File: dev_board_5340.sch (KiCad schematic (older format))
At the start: 41 parts, among them J1 Conn_01x04_Male, J2 USB_C_Receptacle_USB2.0, U1 nrf5340, U2 USBLC6-2SC6, U3 W25Q128JVS, Y1 Crystal_GND2_Small

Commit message: change schematic
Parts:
- added AE?: Antenna, symbol Device:Antenna
- added C? (x8): C_Small, symbol Device:C_Small
- added J?: Conn_01x02_Male, symbol Connector:Conn_01x02_Male
- added L? (x2): INDUCTOR, symbol pspice:INDUCTOR
- added R? (x3): R_Small, symbol Device:R_Small
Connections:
- net labels added: B_LED, DCC, G_LED, R_LED, USER_BUT
- wire segments 174 -> 213
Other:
- moved on the sheet: AE1, C?, D1, R1, R2, R3, R?, SW?, Y?

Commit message: change schematic
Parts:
- added C14, C25, C26, C27, C? (x3): C_Small, symbol Device:C_Small
- added D? (x3): LED, symbol Device:LED
- added J? (x2): Conn_01x24, symbol Connector_Generic:Conn_01x24
- added R? (x3): R_Small, symbol Device:R_Small
- added U4, U?: AZ1117-3.3, symbol Regulator_Linear:AZ1117-3.3
- gave numbers to parts that had none: 22
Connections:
- net labels added: +VDC, P0.10, P0.11, P0.12, P0.23, P0.24, P0.25, P0.26, P0.27, P0.28, P0.29, P0.30, P0.31, P0.4, P0.5, P0.6, P0.7, P0.8, P0.9, P1.0, P1.1, P1.10, P1.11, P1.12, P1.13, P1.14, P1.15, P1.2, P1.3, P1.4, P1.5, P1.6, P1.7, P1.8, P1.9
- wire segments 213 -> 346
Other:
- moved on the sheet: D1, D2, D3, D4, F1, J2, R1, R13, R2, R3, R4, R5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

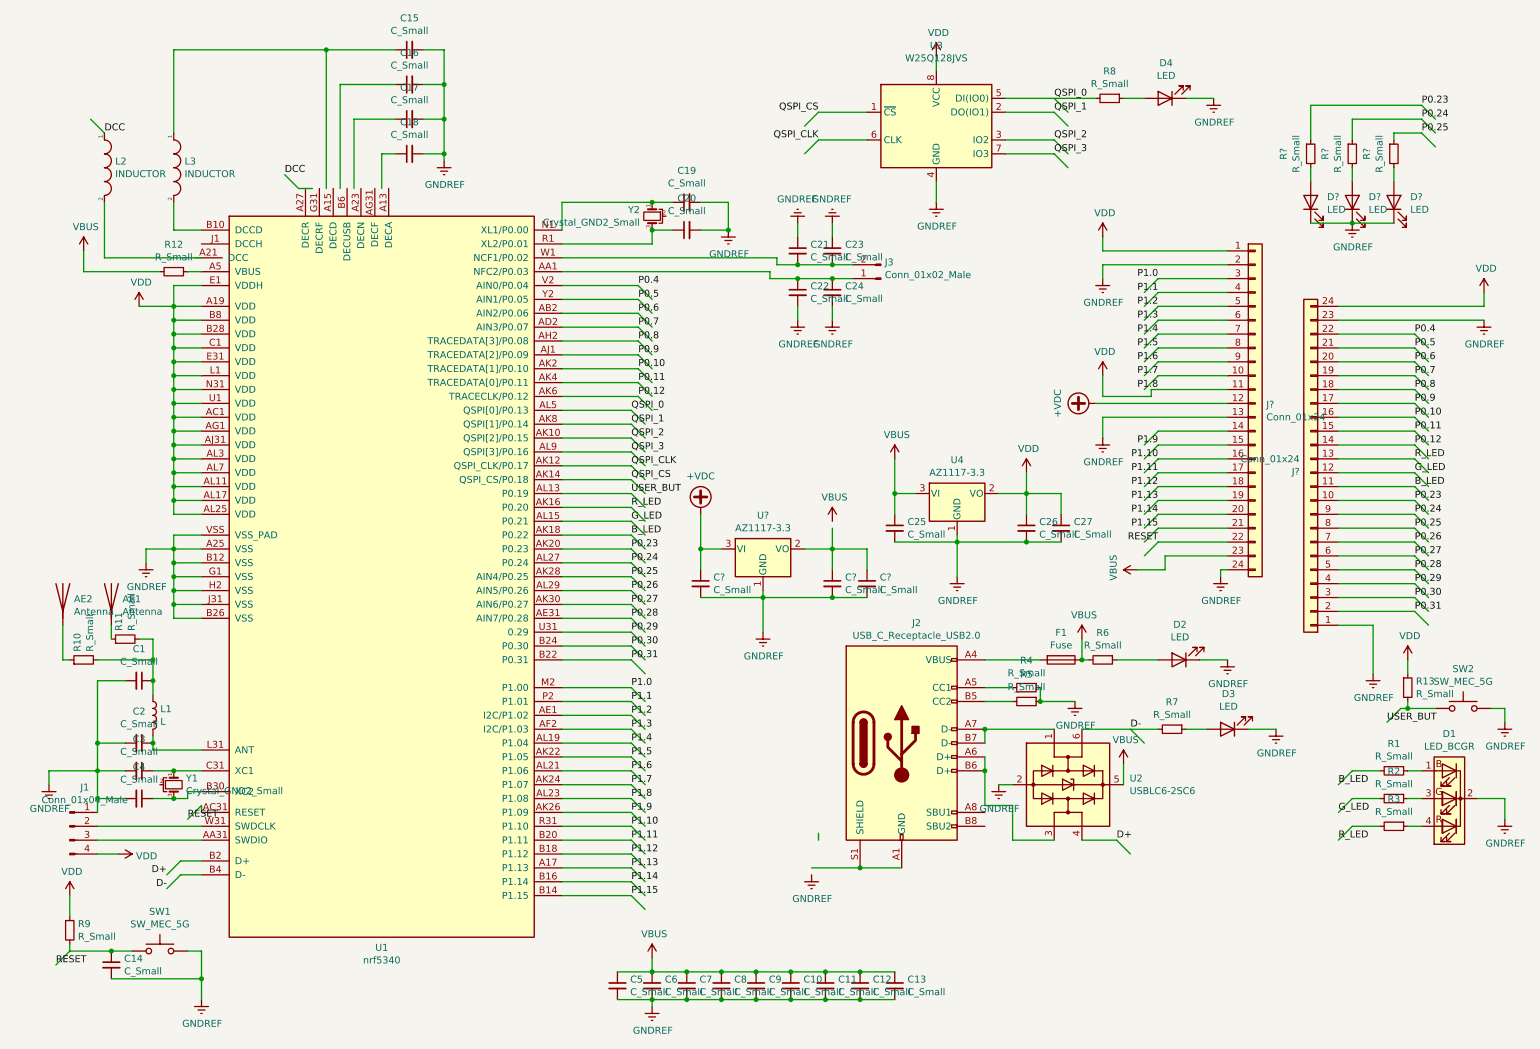
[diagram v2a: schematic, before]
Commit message: add footprint and rating for each component
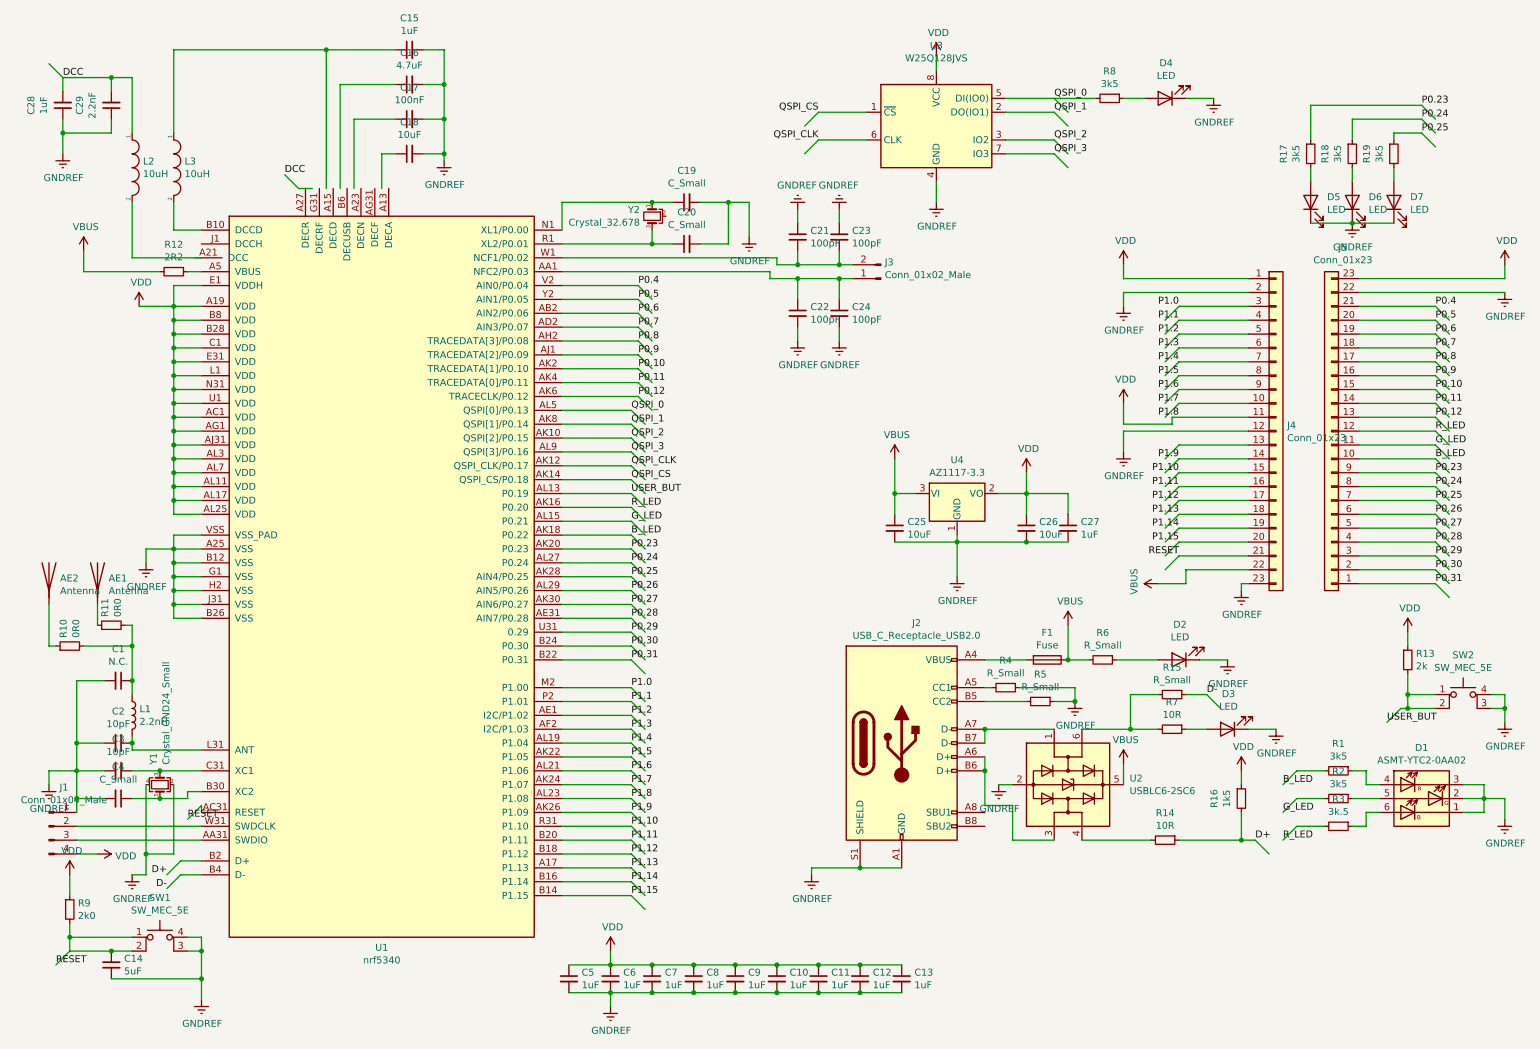
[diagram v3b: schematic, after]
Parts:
- removed C? (x3): C_Small, symbol Device:C_Small
- removed D1: LED_BCGR, symbol Device:LED_BCGR
- removed J? (x2): Conn_01x24, symbol Connector_Generic:Conn_01x24
- removed SW1, SW2: SW_MEC_5G, symbol Switch:SW_MEC_5G
- removed U?: AZ1117-3.3, symbol Regulator_Linear:AZ1117-3.3
- removed Y1: Crystal_GND2_Small, symbol Device:Crystal_GND2_Small
- added C28: 1uF, Capacitor_SMD:C_0805_2012Metric, symbol Device:C_Small
- added C29: 2.2nF, Capacitor_SMD:C_0805_2012Metric, symbol Device:C_Small
- added D1: ASMT-YTC2-0AA02, LED_SMD:LED_Avago_PLCC6_3x2.8mm, symbol LED:ASMT-YTC2-0AA02
- added J4, J5: Conn_01x23, Connector_PinHeader_2.54mm:PinHeader_1x23_P2.54mm_Vertical, symbol Connector_Generic:Conn_01x23
- added R14: 10R, Resistor_SMD:R_1206_3216Metric, symbol Device:R_Small
- added R15: R_Small, Resistor_SMD:R_1206_3216Metric, symbol Device:R_Small
- added R16: 1k5, Capacitor_SMD:C_0805_2012Metric, symbol Device:R_Small
- added SW1, SW2: SW_MEC_5E, Button_Switch_SMD:SW_Push_1P1T_NO_CK_KSC6xxJ, symbol Switch:SW_MEC_5E
- added Y1: Crystal_GND24_Small, Crystal:Crystal_SMD_3225-4Pin_3.2x2.5mm, symbol Device:Crystal_GND24_Small
- AE1: footprint (none) -> RF_Antenna:Texas_SWRA117D_2.4GHz_Left
- AE2: footprint (none) -> Connector_Coaxial:U.FL_Hirose_U.FL-R-SMT-1_Vertical
- C1: value C_Small -> N.C.; footprint (none) -> Capacitor_SMD:C_0805_2012Metric
- C10, C11, C12, C13, C15, C27, C5, C6, C7, C8, C9: value C_Small -> 1uF; footprint (none) -> Capacitor_SMD:C_0805_2012Metric
- C14: value C_Small -> 5uF; footprint (none) -> Capacitor_SMD:C_0805_2012Metric
- C16: value C_Small -> 4.7uF; footprint (none) -> Capacitor_SMD:C_0805_2012Metric
- C17: value C_Small -> 100nF; footprint (none) -> Capacitor_SMD:C_0805_2012Metric
- C18: value C_Small -> 10uF; footprint (none) -> Capacitor_SMD:C_0805_2012Metric
- C19, C20, C4: footprint (none) -> Capacitor_SMD:C_0805_2012Metric
- C2, C3: value C_Small -> 10pF; footprint (none) -> Capacitor_SMD:C_0805_2012Metric
- C21, C22, C23, C24: value C_Small -> 100pF; footprint (none) -> Capacitor_SMD:C_0805_2012Metric
- C25, C26: value C_Small -> 10uF; footprint (none) -> Capacitor_SMD:C_1206_3216Metric
- D2, D3, D4: footprint (none) -> Diode_SMD:D_0805_2012Metric
- D5, D6, D7: renamed from D?; footprint (none) -> Diode_SMD:D_0805_2012Metric
- F1: footprint (none) -> Fuse:Fuse_1206_3216Metric
- J1: footprint (none) -> Connector_PinHeader_2.54mm:PinHeader_1x04_P2.54mm_Vertical
- J2: footprint (none) -> Connector_USB:USB_C_Receptacle_XKB_U262-16XN-4BVC11
- J3: footprint (none) -> Connector_PinHeader_2.54mm:PinHeader_1x02_P2.54mm_Vertical
- L1: value L -> 2.2nH; footprint (none) -> Inductor_SMD:L_1206_3216Metric
- L2, L3: value INDUCTOR -> 10uH; footprint (none) -> Inductor_SMD:L_1206_3216Metric
- R1, R2, R8: value R_Small -> 3k5; footprint (none) -> Resistor_SMD:R_0805_2012Metric
- R10, R11: value R_Small -> 0R0; footprint (none) -> Resistor_SMD:R_0402_1005Metric
- R12: value R_Small -> 2R2; footprint (none) -> Resistor_SMD:R_1206_3216Metric
- R13: value R_Small -> 2k; footprint (none) -> Capacitor_SMD:C_0805_2012Metric
- R17, R18, R19: renamed from R?; value R_Small -> 3k5; footprint (none) -> Resistor_SMD:R_0805_2012Metric
- R3: value R_Small -> 3k.5; footprint (none) -> Resistor_SMD:R_0805_2012Metric
- R4, R5: footprint (none) -> Resistor_SMD:R_0805_2012Metric
- R6: footprint (none) -> Resistor_SMD:R_1206_3216Metric
- R7: value R_Small -> 10R; footprint (none) -> Capacitor_SMD:C_0805_2012Metric
- R9: value R_Small -> 2k0; footprint (none) -> Resistor_SMD:R_0805_2012Metric
- U4: footprint (none) -> Package_TO_SOT_SMD:SOT-223
- Y2: value Crystal_GND2_Small -> Crystal_32.678; footprint (none) -> Crystal:Crystal_SMD_3215-2Pin_3.2x1.5mm
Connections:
- net B_LED: now also J5.10 (Pin_10)
- net D+: now also R14.1, R16.2; no longer U2.4 (I/O2)
- net D-: now also R15.1; no longer R7.2, U2.6 (I/O1)
- net DCC: now also C28.2, C29.2
- net GNDREF: now also J2.A1 (GND), J2.A12 (GND), J2.B1 (GND), J2.B12 (GND), J2.S1 (SHIELD), C28.1, C29.1, D1.1 (KB), D1.2 (KG), D1.3 (KR), J4.12 (Pin_12), J4.2 (Pin_2), J4.23 (Pin_23), J5.22 (Pin_22), SW1.3 (K), SW1.4 (A), SW2.3 (K), SW2.4 (A), Y1.2, Y1.4
- net G_LED: now also J5.11 (Pin_11)
- net P0.10: now also J5.15 (Pin_15)
- net P0.11: now also J5.14 (Pin_14)
- net P0.12: now also J5.13 (Pin_13)
- net P0.23: now also J5.9 (Pin_9)
- net P0.24: now also J5.8 (Pin_8)
- net P0.25: now also J5.7 (Pin_7)
- net P0.26: now also J5.6 (Pin_6)
- net P0.27: now also J5.5 (Pin_5)
- net P0.28: now also J5.4 (Pin_4)
- net P0.29: now also J5.3 (Pin_3)
- net P0.30: now also J5.2 (Pin_2)
- net P0.31: now also J5.1 (Pin_1)
- net P0.4: now also J5.21 (Pin_21)
- net P0.5: now also J5.20 (Pin_20)
- net P0.6: now also J5.19 (Pin_19)
- net P0.7: now also J5.18 (Pin_18)
- net P0.8: now also J5.17 (Pin_17)
- net P0.9: now also J5.16 (Pin_16)
- net P1.0: now also J4.3 (Pin_3)
- net P1.1: now also J4.4 (Pin_4)
- net P1.10: now also J4.15 (Pin_15)
- net P1.11: now also J4.16 (Pin_16)
- net P1.12: now also J4.17 (Pin_17)
- net P1.13: now also J4.18 (Pin_18)
- net P1.14: now also J4.19 (Pin_19)
- net P1.15: now also J4.20 (Pin_20)
- net P1.2: now also J4.5 (Pin_5)
- net P1.3: now also J4.6 (Pin_6)
- net P1.4: now also J4.7 (Pin_7)
- net P1.5: now also J4.8 (Pin_8)
- net P1.6: now also J4.9 (Pin_9)
- net P1.7: now also J4.10 (Pin_10)
- net P1.9: now also J4.14 (Pin_14)
- net RESET: now also J4.21 (Pin_21)
- net R_LED: now also J5.12 (Pin_12)
- net VBUS: now also J4.22 (Pin_22); no longer C10.1, C11.1, C12.1, C13.1, C5.1, C6.1, C7.1, C8.1, C9.1
- net VDD: now also C10.1, C11.1, C12.1, C13.1, C5.1, C6.1, C7.1, C8.1, C9.1, J4.1 (Pin_1), J4.11 (Pin_11), J5.23 (Pin_23), R16.1
- net at C4.1, U1.B30 (XC2): now also Y1.1
- net at C3.1, U1.C31 (XC1): now also Y1.3
- net at R1.1: now also D1.4 (AR)
- net at R2.1: now also D1.5 (AG)
- net at R3.1: now also D1.6 (AB)
- net at C14.1, R9.2: now also SW1.1, SW1.2
- net at R13.2: now also SW2.1, SW2.2
- new net: R14.2, U2.4 (I/O2)
- new net: R15.2, R7.2, U2.6 (I/O1)
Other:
- moved on the sheet: AE1, AE2, C1, C10, C11, C12, C13, C2, C20, C21, C22, C23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

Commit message: Refactoring. Start trace
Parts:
- removed SW1, SW2: SW_MEC_5E, Button_Switch_SMD:SW_Push_1P1T_NO_CK_KSC6xxJ, symbol Switch:SW_MEC_5E
- removed Y2: Crystal_32.678, Crystal:Crystal_SMD_3215-2Pin_3.2x1.5mm, symbol Device:Crystal_GND2_Small
- added SW1, SW2: SW_Push_Dual_x2, Button_Switch_SMD:SW_Push_1P1T_NO_CK_KSC6xxJ, symbol Switch:SW_Push_Dual_x2
- added Y2: Crystal_Small, Crystal:Crystal_SMD_3215-2Pin_3.2x1.5mm, symbol Device:Crystal_Small
- C10, C11, C12, C13, C17, C28, C29, C5, C6, C8, C9: footprint Capacitor_SMD:C_0805_2012Metric -> Capacitor_SMD:C_0402_1005Metric
- D2, D3, D4, D5, D6, D7: footprint Diode_SMD:D_0805_2012Metric -> Diode_SMD:D_0603_1608Metric
- R1, R17, R18, R19, R2, R3, R8: footprint Resistor_SMD:R_0805_2012Metric -> Resistor_SMD:R_0603_1608Metric
- R13, R16: footprint Capacitor_SMD:C_0805_2012Metric -> Resistor_SMD:R_0402_1005Metric
- R15: value R_Small -> 10R
- R6: footprint Resistor_SMD:R_1206_3216Metric -> Resistor_SMD:R_0603_1608Metric
- R7: value 10R -> 3k; footprint Capacitor_SMD:C_0805_2012Metric -> Resistor_SMD:R_0603_1608Metric
- R9: footprint Resistor_SMD:R_0805_2012Metric -> Resistor_SMD:R_0402_1005Metric
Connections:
- net GNDREF: now also SW1.2 (D), SW2.2 (D)
- net at U1.A13 (DECA): now also C18.1
- net at U1.A15 (DECD): now also C15.1, L3.1
- net at U1.A21 (DCC): now also L2.2
- net at U1.A23 (DECN): now also C17.1
- net at U1.A27 (DECR): now also U1.G31 (DECRF)
- net at U1.B6 (DECUSB): now also C16.1
- net at C19.1, U1.N1 (XL1/P0.00): now also Y2.2
- net at C20.1, U1.R1 (XL2/P0.01): now also Y2.1
- net at C14.1, R9.2: now also SW1.1 (C)
- net at R13.2: now also SW2.1 (C)
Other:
- moved on the sheet: C18

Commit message: Delete test usb net
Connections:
- net VDD: no longer U1.AL23 (P1.08)
- net P1.8: now reaches J4.13 (Pin_13)
- net P1.8: now also U1.AL23 (P1.08)
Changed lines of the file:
@@
 Text Label 8750 3250 2    50   ~ 0
 P1.7
-Text Label 8750 3350 2    50   ~ 0
+Text Label 8750 3550 2    50   ~ 0
 P1.8
 Entry Wire Line
